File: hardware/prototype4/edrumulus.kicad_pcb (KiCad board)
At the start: 2 copper layers, 65 x 56.5 mm, 67 parts, among them J1 Trigger Connector, J2 Raspberry Pi GPIO pins, U1 ESP32-DEVKIT-V1

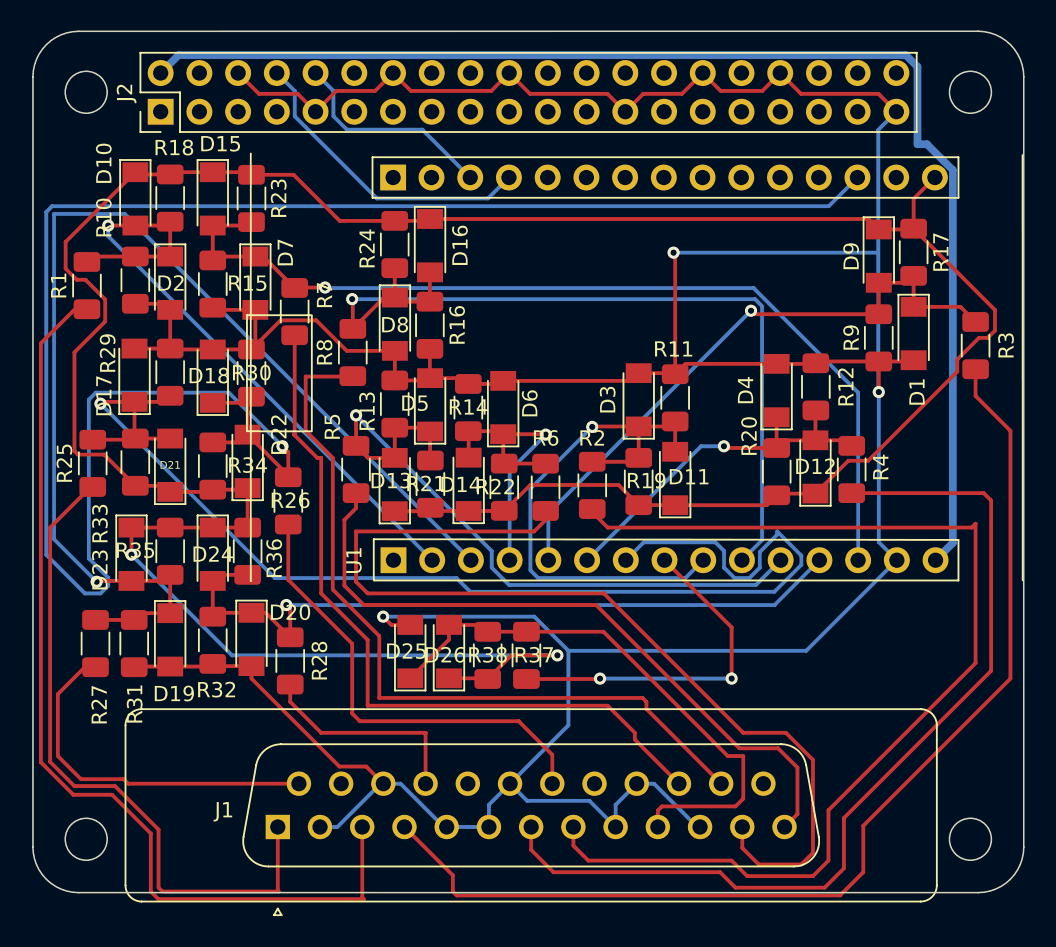
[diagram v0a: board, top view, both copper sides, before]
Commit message: fix some warnings
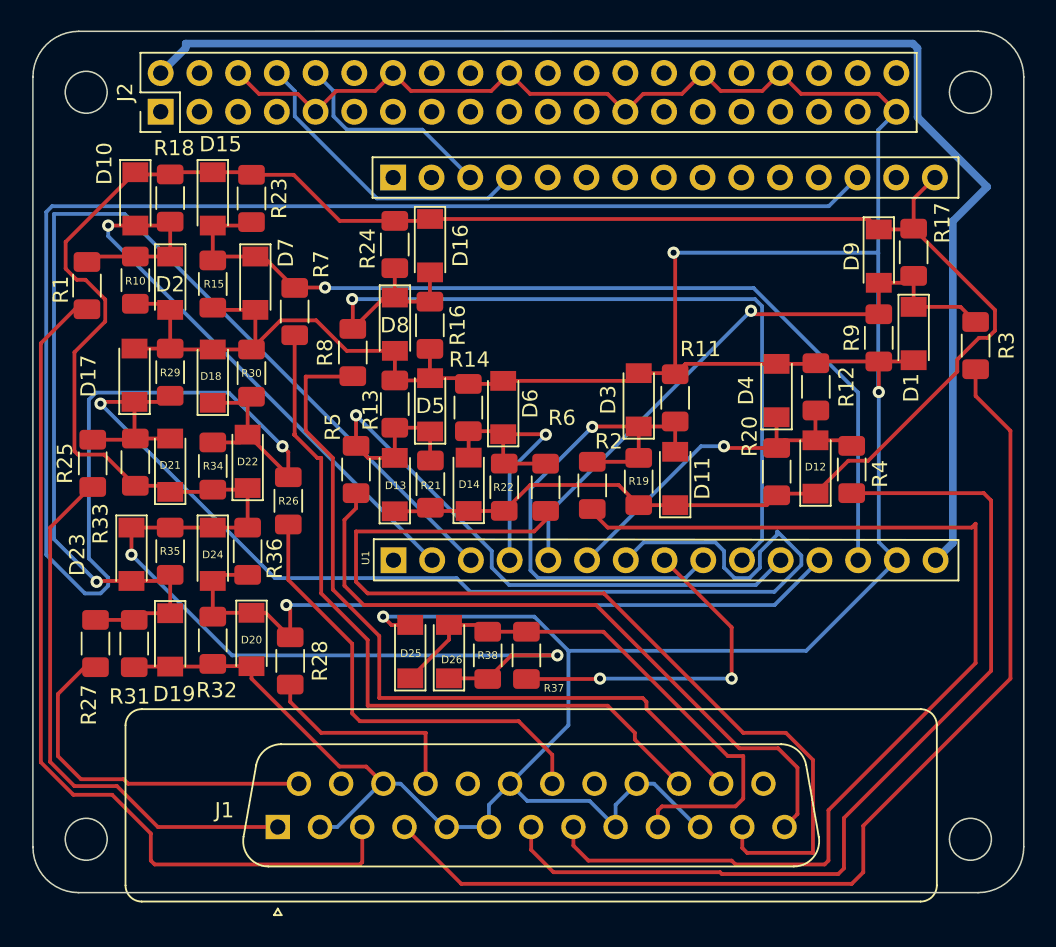
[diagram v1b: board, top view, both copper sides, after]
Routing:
- net KICK-TIP: track 44.3 -> 36.0 mm
- net SNARE-TIP: track 63.3 -> 58.7 mm
- net ESP-VIN: track 84.6 -> 87.6 mm
- net SNARE-RING: track 71.1 -> 69.9 mm
- net HI-HAT-TIP: track 61.0 -> 60.3 mm
- net CRASH1-TIP: track 64.3 -> 63.7 mm
- net HI-HAT-RING: track 71.2 -> 70.5 mm

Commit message: optimize connections for prototype 4
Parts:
- moved R24 11.6 mm to (141.5, 90.2), turned to 180 degrees
- moved D16 8.90 mm to (141.5, 87.6), turned to 180 degrees
- moved R16 5.09 mm to (137.4, 90.7)
- moved D8 4.78 mm to (134.9, 90.9)
- moved R7 3.03 mm to (125.5, 94.0)
- moved D2 2.03 mm to (117.6, 89.7)
- moved R18 2.03 mm to (117.6, 84.0)
- moved R10 1.80 mm to (115.1, 89.7)
- moved D10 1.79 mm to (115.1, 84.3)
- moved D15 1.79 mm to (120.1, 84.3)
- moved R23 1.79 mm to (122.7, 84.1)
- moved R15 1.78 mm to (120.1, 89.7)
- moved R14 1.68 mm to (135.9, 96.3)
- moved D6 1.65 mm to (138.4, 96.5)
- moved D7 1.52 mm to (122.7, 89.6)
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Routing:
- net CRASH1-SLEEVE: track 276.5 -> 348.8 mm
- net 3V3: track 197.5 -> 206.6 mm
- net TOM1-TIP: track 23.8 -> 16.1 mm
- net GPIO27: track 56.1 -> 62.6 mm
- net SNARE-TIP: track 58.7 -> 52.3 mm
- net KICK-TIP: track 36.0 -> 30.8 mm
- net GPIO13: track 62.1 -> 66.5 mm
- net RIDE-RING: track 49.6 -> 45.4 mm
- net HI-HAT-CONTROL-TIP: track 37.2 -> 33.4 mm
- net RIDE-TIP: track 51.2 -> 47.4 mm
- net GPIO14: track 45.0 -> 47.2 mm
- net TOM3-TIP: track 30.3 -> 28.8 mm
- net TOM2-TIP: track 14.2 -> 13.0 mm
- net ESP-VIN: track 87.6 -> 86.6 mm
- net GPIO39: track 74.7 -> 73.9 mm
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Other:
- board text added: "Edrumulus Prototype 4"

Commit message: some more optimizations for prototype 4
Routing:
- net GPIO15: track 123.5 -> 127.4 mm
- net ESP-UART0-RX: track 20.2 -> 22.0 mm
- net GPIO33: track 81.2 -> 82.9 mm
- net CRASH1-SLEEVE: track 348.8 -> 350.1 mm
- net GPIO14: track 47.2 -> 47.8 mm
- net GPIO26: track 35.9 -> 36.4 mm
- net ESP-UART0-TX: track 14.0 -> 14.5 mm

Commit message: added filler
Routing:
- added copper zone on B.Cu, net CRASH1-SLEEVE
- added copper zone on F.Cu, net CRASH1-SLEEVE
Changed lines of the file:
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@@
   (via (at 143.764 115.57) (size 0.8) (drill 0.4) (layers "F.Cu" "B.Cu") (net 64))
   (segment (start 143.764 115.57) (end 152.4 115.57) (width 0.25) (layer "B.Cu") (net 64))
+  (zone (net 1) (net_name "CRASH1-SLEEVE") (layer "F.Cu") (hatch edge 0.508)
+    (connect_pads (clearance 0.508))
+    (min_thickness 0.254) (filled_areas_thickness no)
+    (fill yes (thermal_gap 0.508) (thermal_bridge_width 0.508))
+    (polygon
+      (pts
+        (xy 171.561542 129.601205)
+        (xy 106.68 129.794)
+        (xy 106.584157 73.107062)
+        (xy 171.704 73.152)
+      )
+    )
+  )
+  (zone (net 1) (net_name "CRASH1-SLEEVE") (layer "B.Cu") (hatch edge 0.508)
+    (connect_pads (clearance 0.508))
+    (min_thickness 0.254) (filled_areas_thickness no)
+    (fill yes (thermal_gap 0.508) (thermal_bridge_width 0.508))
+    (polygon
+      (pts
+        (xy 171.573414 129.597233)
+        (xy 106.595381 129.584665)
+        (xy 106.426 73.152)
+        (xy 171.580429 73.096443)
+      )
+    )
+  )
   (group "" locked (id 1d468920-09d8-44ff-9425-46d8affb1930)
     (members

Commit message: added an additional GND to the ESP32 board
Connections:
- U1 pad 17: unconnected-(U1-Pad17) -> CRASH1-SLEEVE
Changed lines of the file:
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@@
   (net 64 "GPIO25")
   (net 65 "unconnected-(U1-Pad1)")
-  (net 66 "unconnected-(U1-Pad17)")
-  (net 67 "unconnected-(U1-Pad19)")
-  (net 68 "unconnected-(U1-Pad20)")
-  (net 69 "unconnected-(U1-Pad21)")
-  (net 70 "unconnected-(U1-Pad22)")
-  (net 71 "unconnected-(U1-Pad23)")
-  (net 72 "unconnected-(U1-Pad24)")
-  (net 73 "unconnected-(U1-Pad25)")
-  (net 74 "unconnected-(U1-Pad26)")
-  (net 75 "unconnected-(U1-Pad29)")
-  (net 76 "unconnected-(U1-Pad30)")
+  (net 66 "unconnected-(U1-Pad19)")
+  (net 67 "unconnected-(U1-Pad20)")
+  (net 68 "unconnected-(U1-Pad21)")
+  (net 69 "unconnected-(U1-Pad22)")
+  (net 70 "unconnected-(U1-Pad23)")
+  (net 71 "unconnected-(U1-Pad24)")
+  (net 72 "unconnected-(U1-Pad25)")
+  (net 73 "unconnected-(U1-Pad26)")
+  (net 74 "unconnected-(U1-Pad29)")
+  (net 75 "unconnected-(U1-Pad30)")
   (footprint "Diode_SMD:D_MiniMELF" (layer "F.Cu")
     (at 164.338 92.936 -90)
@@
       (net 10 "3V3") (pinfunction "3V3") (pintype "output"))
     (pad "17" thru_hole oval (at 25.124 32.998 270) (size 1.7 1.7) (drill 1) (layers *.Cu *.Mask)
-      (net 66 "unconnected-(U1-Pad17)") (pinfunction "GND") (pintype "bidirectional+no_connect"))
+      (net 1 "CRASH1-SLEEVE") (pinfunction "GND") (pintype "bidirectional"))
     (pad "18" thru_hole oval (at 25.124 30.458 270) (size 1.7 1.7) (drill 1) (layers *.Cu *.Mask)
       (net 12 "GPIO15") (pinfunction "GPIO15_ADC2-CH3_HSPI-CS0_RTC-GPIO13") (pintype "bidirectional"))
     (pad "19" thru_hole oval (at 25.124 27.918 270) (size 1.7 1.7) (drill 1) (layers *.Cu *.Mask)
-      (net 67 "unconnected-(U1-Pad19)") (pinfunction "GPIO2_ADC2-CH2_RTC-GPIO12") (pintype "bidirectional+no_connect"))
+      (net 66 "unconnected-(U1-Pad19)") (pinfunction "GPIO2_ADC2-CH2_RTC-GPIO12") (pintype "bidirectional+no_connect"))
     (pad "20" thru_hole oval (at 25.124 25.378 270) (size 1.7 1.7) (drill 1) (layers *.Cu *.Mask)
-      (net 68 "unconnected-(U1-Pad20)") (pinfunction "GPIO4_ADC2-CH0_RTC-GPIO10") (pintype "bidirectional+no_connect"))
+      (net 67 "unconnected-(U1-Pad20)") (pinfunction "GPIO4_ADC2-CH0_RTC-GPIO10") (pintype "bidirectional+no_connect"))
     (pad "21" thru_hole oval (at 25.124 22.838 270) (size 1.7 1.7) (drill 1) (layers *.Cu *.Mask)
-      (net 69 "unconnected-(U1-Pad21)") (pinfunction "GPIO16_UART2-RX") (pintype "bidirectional+no_connect"))
+      (net 68 "unconnected-(U1-Pad21)") (pinfunction "GPIO16_UART2-RX") (pintype "bidirectional+no_connect"))
     (pad "22" thru_hole oval (at 25.124 20.298 270) (size 1.7 1.7) (drill 1) (layers *.Cu *.Mask)
-      (net 70 "unconnected-(U1-Pad22)") (pinfunction "GPIO17_UART2-TX") (pintype "bidirectional+no_connect"))
+      (net 69 "unconnected-(U1-Pad22)") (pinfunction "GPIO17_UART2-TX") (pintype "bidirectional+no_connect"))
     (pad "23" thru_hole oval (at 25.124 17.758 270) (size 1.7 1.7) (drill 1) (layers *.Cu *.Mask)
-      (net 71 "unconnected-(U1-Pad23)") (pinfunction "GPIO5_VSPI-CS0") (pintype "bidirectional+no_connect"))
+      (net 70 "unconnected-(U1-Pad23)") (pinfunction "GPIO5_VSPI-CS0") (pintype "bidirectional+no_connect"))
     (pad "24" thru_hole oval (at 25.124 15.218 270) (size 1.7 1.7) (drill 1) (layers *.Cu *.Mask)
-      (net 72 "unconnected-(U1-Pad24)") (pinfunction "GPIO18_VSPI-CLK") (pintype "bidirectional+no_connect"))
+      (net 71 "unconnected-(U1-Pad24)") (pinfunction "GPIO18_VSPI-CLK") (pintype "bidirectional+no_connect"))
     (pad "25" thru_hole oval (at 25.124 12.678 270) (size 1.7 1.7) (drill 1) (layers *.Cu *.Mask)
-      (net 73 "unconnected-(U1-Pad25)") (pinfunction "GPIO19_VSPI-MISO") (pintype "bidirectional+no_connect"))
+      (net 72 "unconnected-(U1-Pad25)") (pinfunction "GPIO19_VSPI-MISO") (pintype "bidirectional+no_connect"))
     (pad "26" thru_hole oval (at 25.124 10.138 270) (size 1.7 1.7) (drill 1) (layers *.Cu *.Mask)
-      (net 74 "unconnected-(U1-Pad26)") (pinfunction "GPIO21_I2C-SDA") (pintype "bidirectional+no_connect"))
+      (net 73 "unconnected-(U1-Pad26)") (pinfunction "GPIO21_I2C-SDA") (pintype "bidirectional+no_connect"))
     (pad "27" thru_hole oval (at 25.124 7.598 270) (size 1.7 1.7) (drill 1) (layers *.Cu *.Mask)
       (net 57 "ESP-UART0-RX") (pinfunction "GPIO3__UART0-RX") (pintype "bidirectional"))
@@
       (net 56 "ESP-UART0-TX") (pinfunction "GPIO1_UART0-TX") (pintype "bidirectional"))
     (pad "29" thru_hole oval (at 25.124 2.518 270) (size 1.7 1.7) (drill 1) (layers *.Cu *.Mask)
-      (net 75 "unconnected-(U1-Pad29)") (pinfunction "GPIO22_I2C-SCL") (pintype "bidirectional+no_connect"))
+      (net 74 "unconnected-(U1-Pad29)") (pinfunction "GPIO22_I2C-SCL") (pintype "bidirectional+no_connect"))
     (pad "30" thru_hole rect (at 25.124 0 270) (size 1.7 1.7) (drill 1) (layers *.Cu *.Mask)
-      (net 76 "unconnected-(U1-Pad30)") (pinfunction "GPIO23_VSPI-MOSI") (pintype "bidirectional+no_connect"))
+      (net 75 "unconnected-(U1-Pad30)") (pinfunction "GPIO23_VSPI-MOSI") (pintype "bidirectional+no_connect"))
     (model "${KICAD6_3DMODEL_DIR}/Connector_PinSocket_2.54mm.3dshapes/PinSocket_1x15_P2.54mm_Vertical.wrl"
       (offset (xyz 0 0 0))

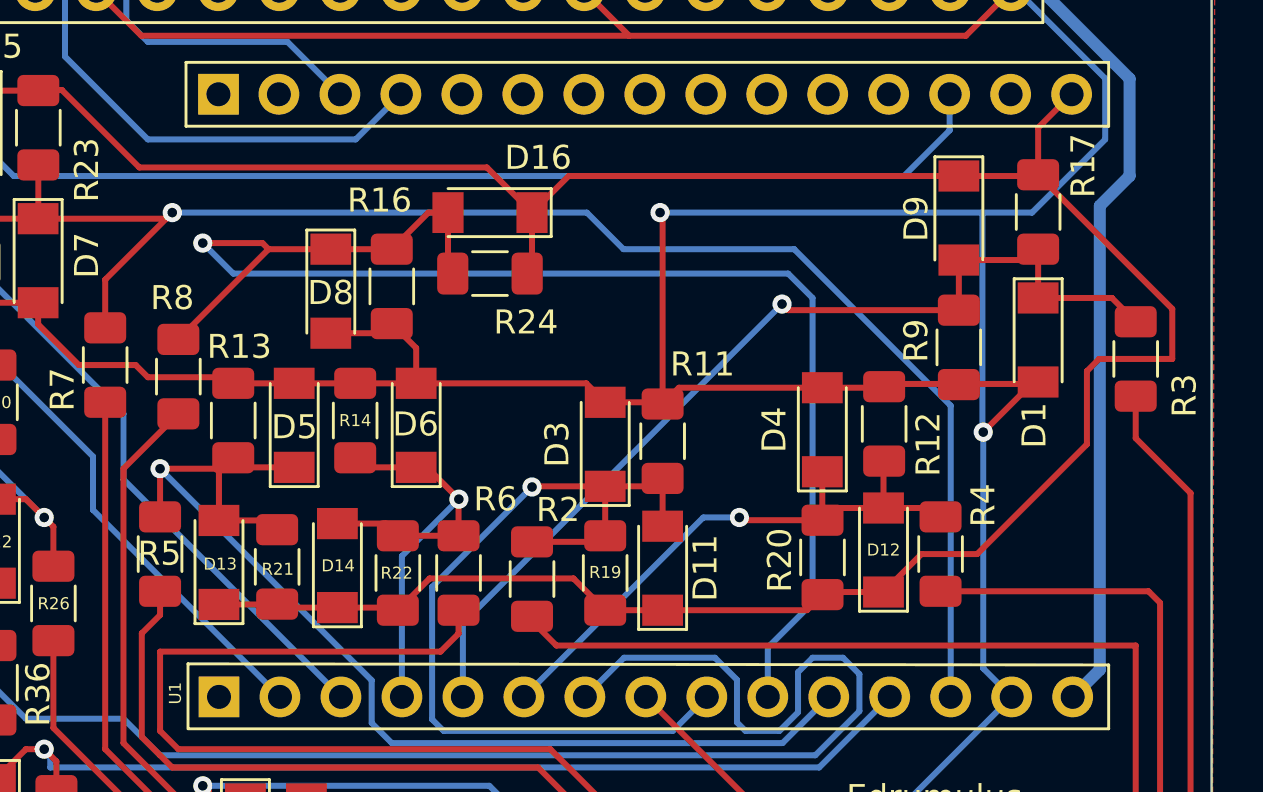
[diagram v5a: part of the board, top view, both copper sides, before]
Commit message: added text for ESP placement
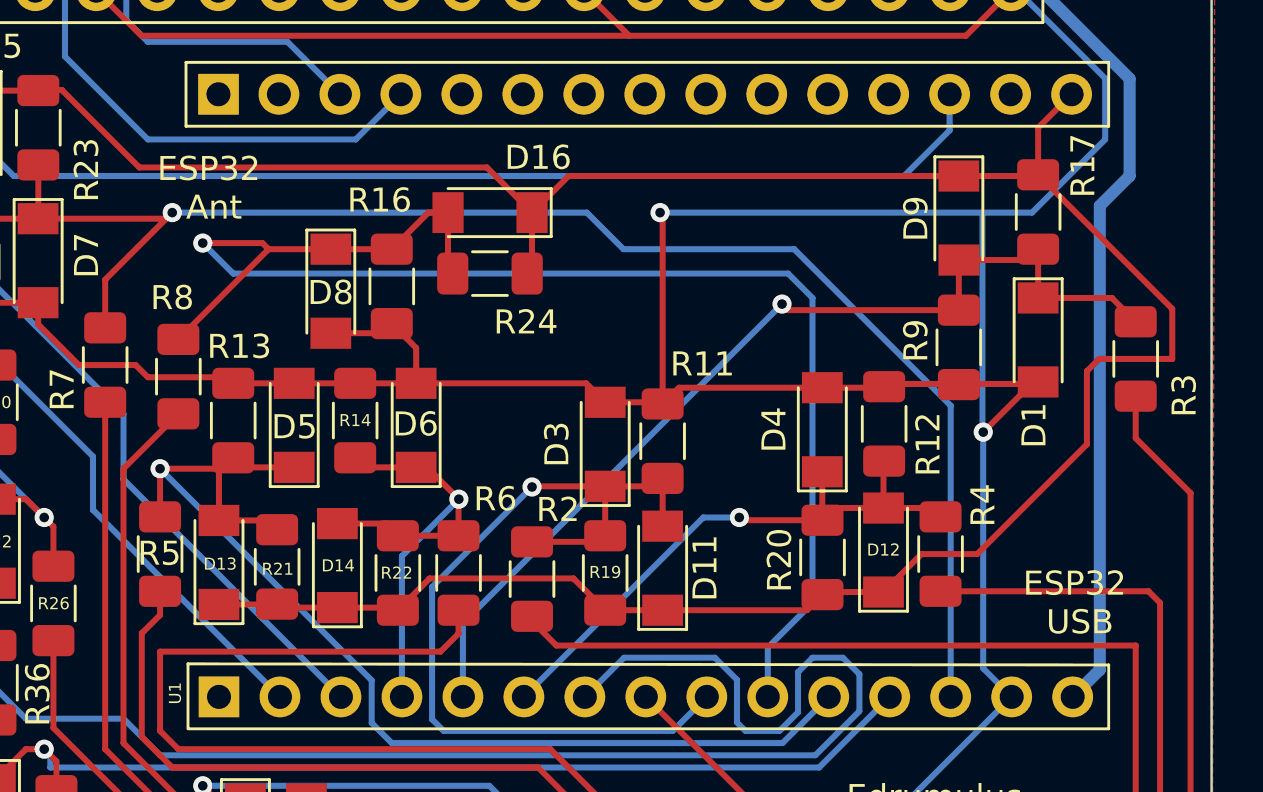
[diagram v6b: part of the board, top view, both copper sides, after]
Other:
- board text added: "ESP32 Ant"
- board text added: "ESP32 USB"
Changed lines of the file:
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@@
   (gr_arc locked (start 109.566816 129.608296) (mid 107.445783 128.730905) (end 106.566194 126.610783) (layer "Edge.Cuts") (width 0.1))
   (gr_circle locked (center 168.062863 126.108162) (end 169.437863 126.108162) (layer "Edge.Cuts") (width 0.1) (fill none))
+  (gr_text "ESP32\n Ant" (at 129.794 86.614) (layer "F.SilkS")
+    (effects (font (size 1 1) (thickness 0.15)))
+  )
   (gr_text "Edrumulus\nPrototype 4" (at 160.02 112.776) (layer "F.SilkS")
     (effects (font (size 1 1) (thickness 0.15)))
   )
+  (gr_text "ESP32\n USB" (at 165.862 103.886) (layer "F.SilkS")
+    (effects (font (size 1 1) (thickness 0.15)))
+  )
